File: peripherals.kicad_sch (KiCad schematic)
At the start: 9 parts, among them U1 MX6UL-VM

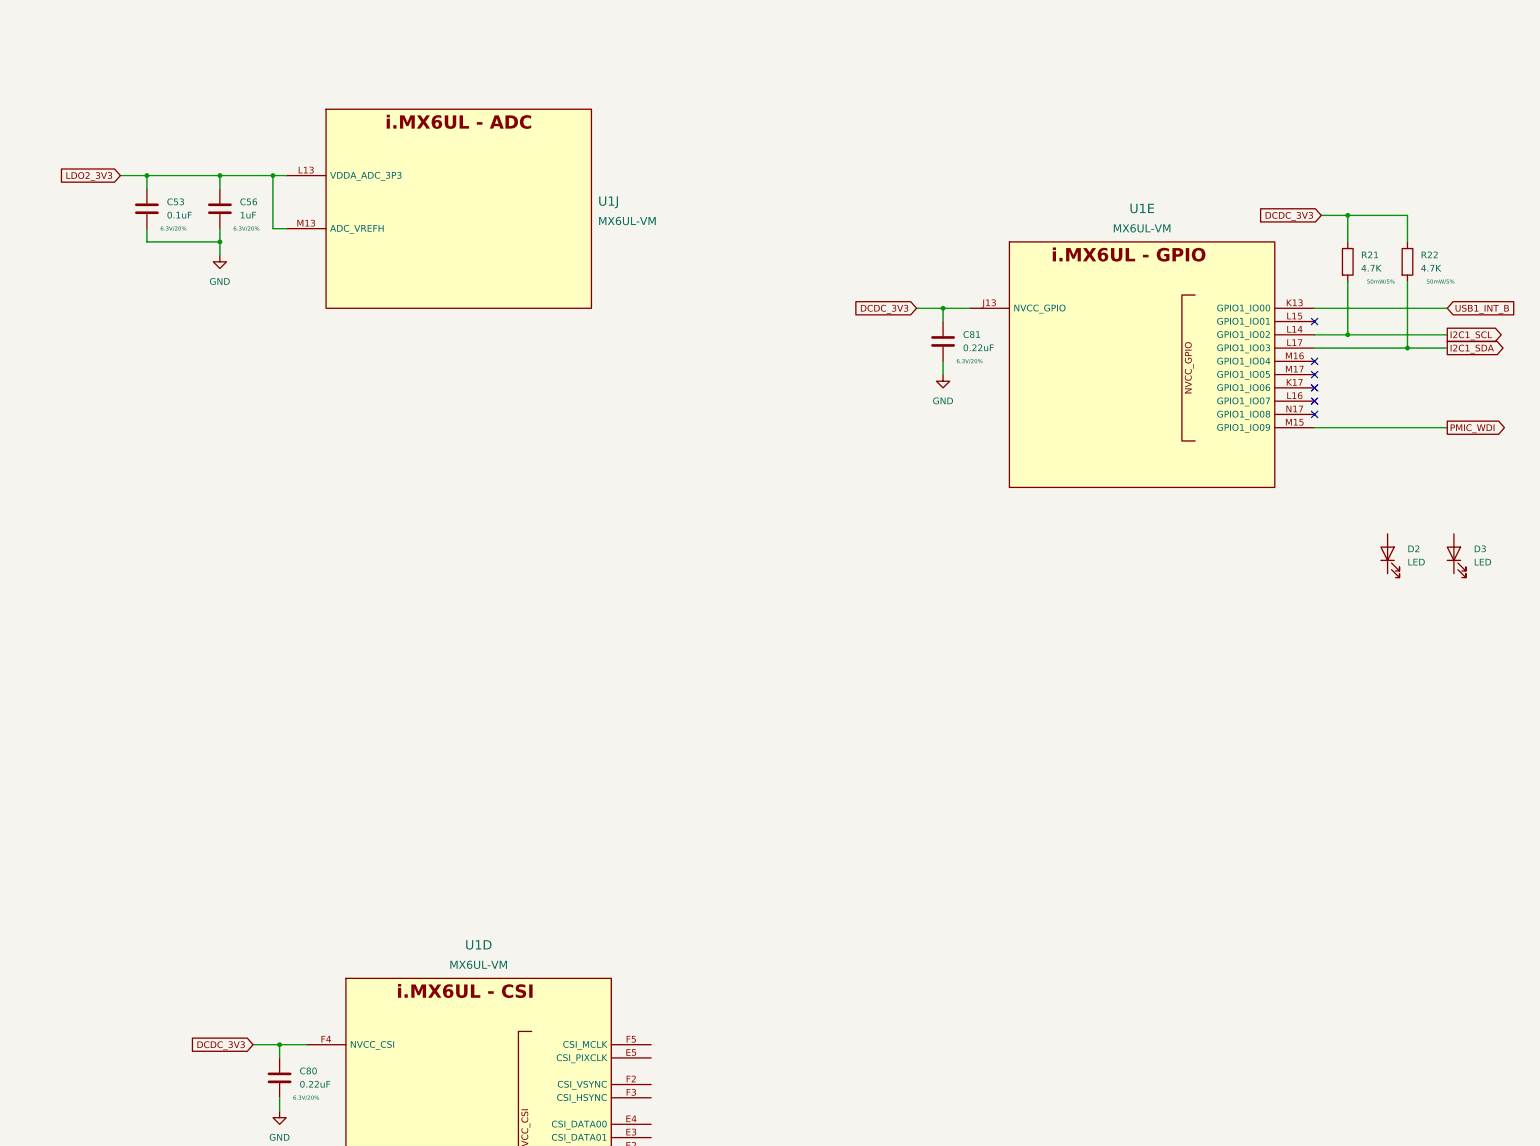
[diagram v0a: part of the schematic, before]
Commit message: start moving to hierarchal labels, add emmc
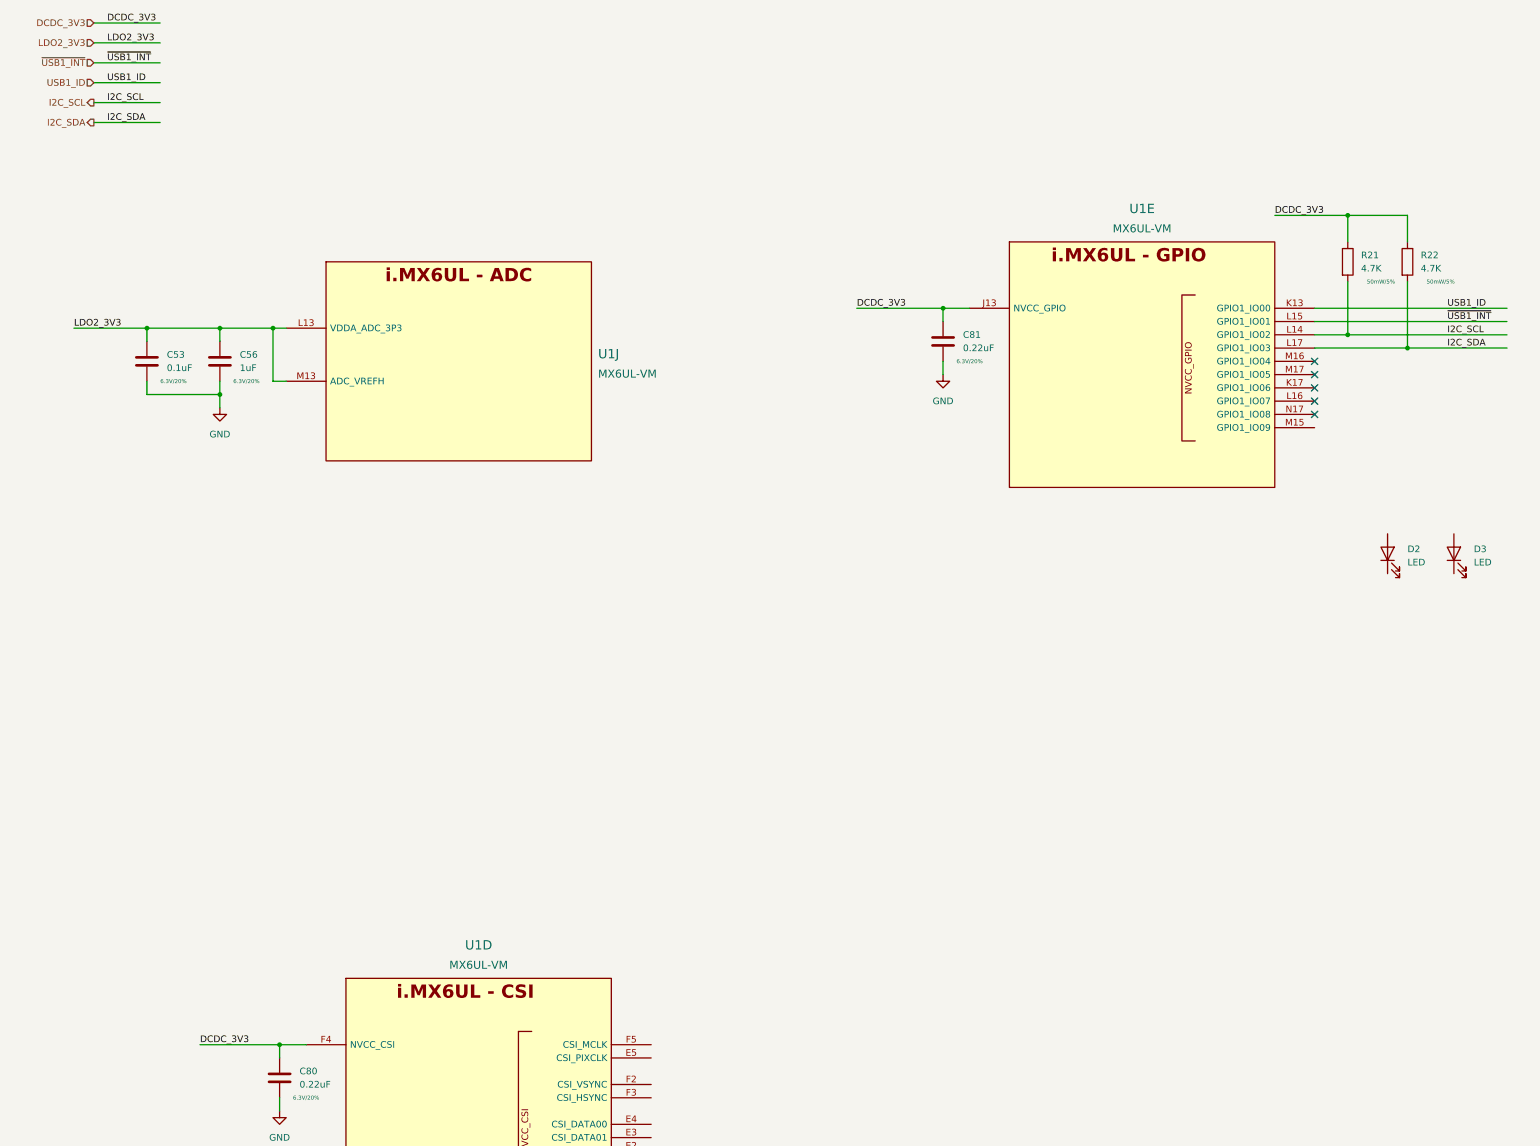
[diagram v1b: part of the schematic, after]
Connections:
- net ~{USB1_INT}: now reaches U1.L15 (GPIO1_IO01)
- net I2C1_SCL renamed I2C_SCL
- net I2C1_SDA renamed I2C_SDA
- net PMIC_WDI: no longer names the net of U1.M15 (GPIO1_IO09)
- net USB1_INT_B renamed USB1_ID
- no-connect marks 6 -> 5
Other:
- moved on the sheet: C53, C56, U1J

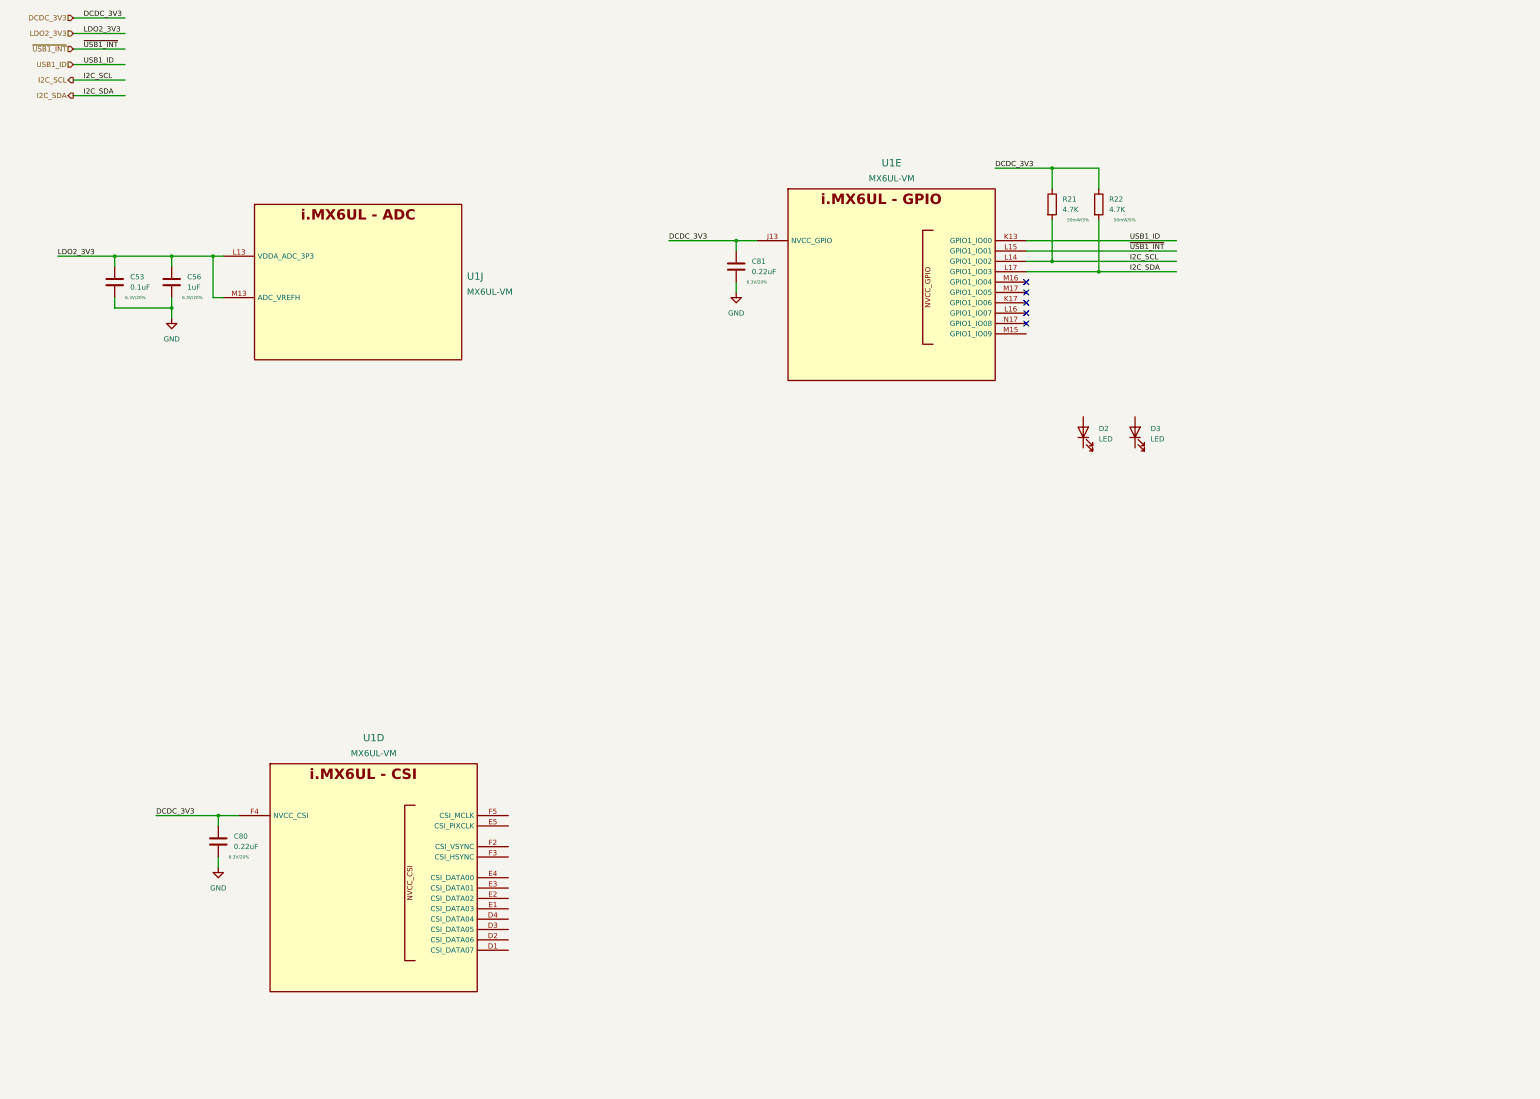
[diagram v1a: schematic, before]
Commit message: move to hierarchal labels, work on power tree, add basic pcb layout
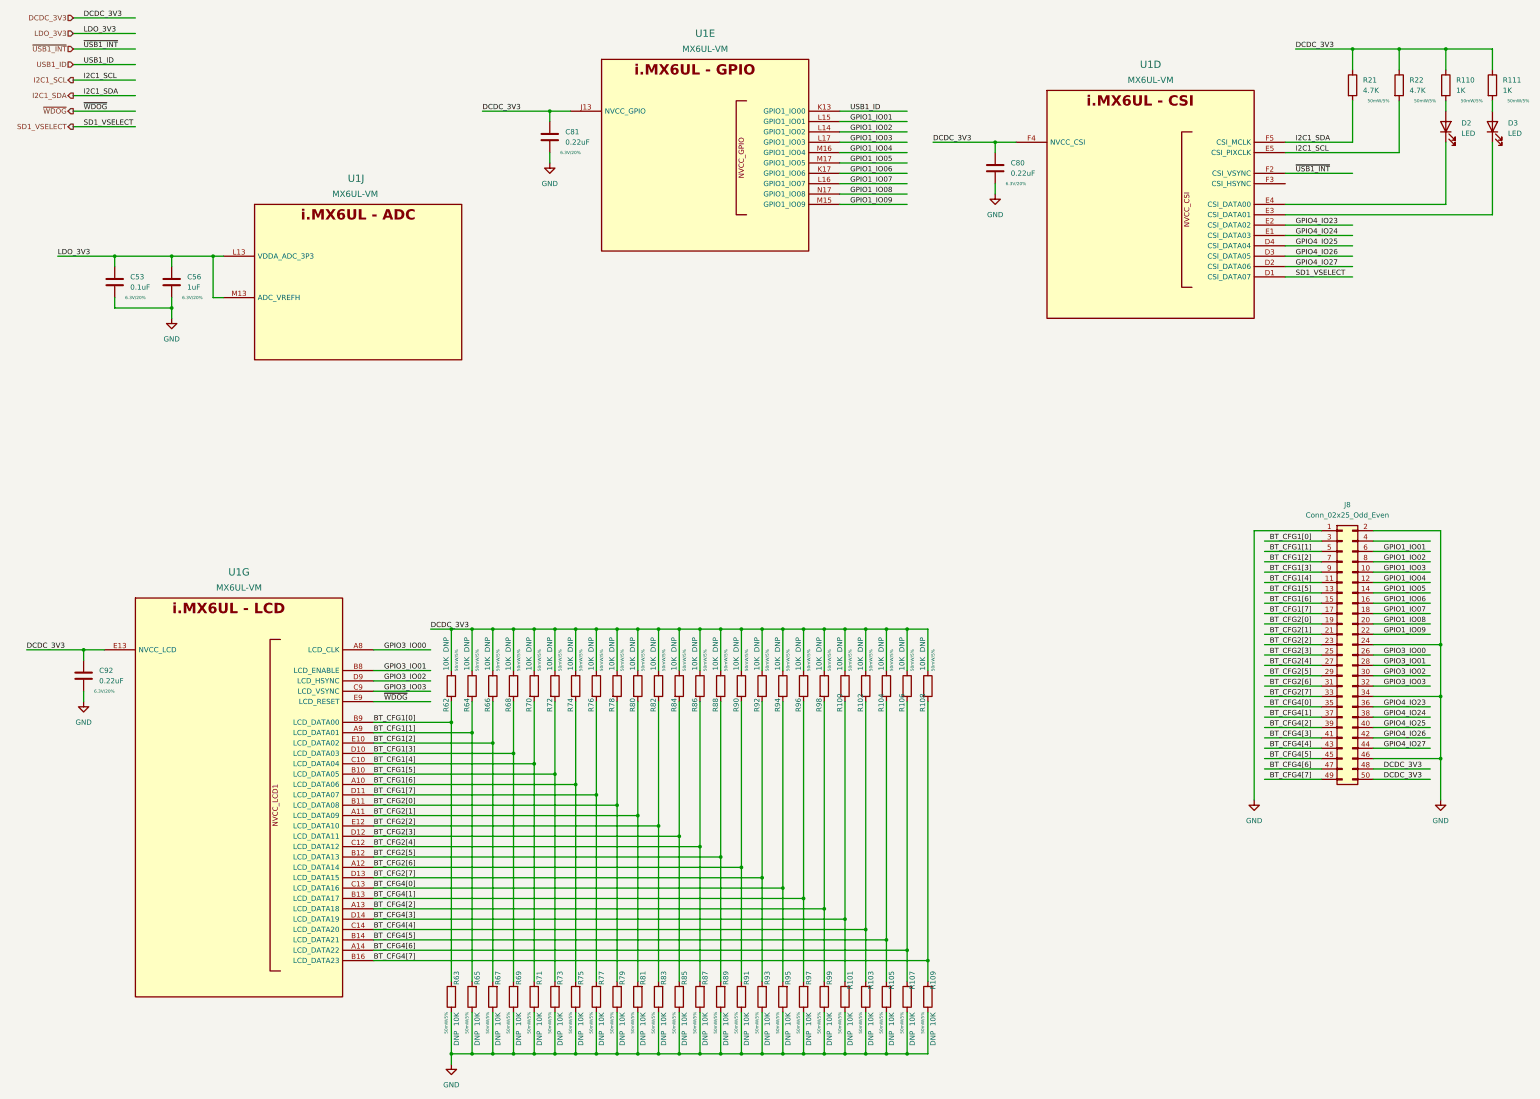
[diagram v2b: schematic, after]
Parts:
- added C92: 0.22uF, Capacitor_SMD:C_0402_1005Metric, symbol Device:C
- added J8: Conn_02x25_Odd_Even, Connector_PinHeader_2.54mm:PinHeader_2x25_P2.54mm_Vertical_SMD, symbol Connector_Generic:Conn_02x25_Odd_Even
- added R100, R101, R102, R103, R104, R105, R106, R107, R108, R109, R62, R63, R64, R65, R66, R67, R68, R69, R70, R71, R72, R73, R74, R75, R76, R77, R78, R79, R80, R81, R82, R83, R84, R85, R86, R87, R88, R89, R90, R91, R92, R93, R94, R95, R96, R97, R98, R99: 10K, Resistor_SMD:R_0402_1005Metric, symbol Device:R
- added R110, R111: 1K, Resistor_SMD:R_0402_1005Metric, symbol Device:R
- added unit 7 of U1
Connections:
- net DCDC_3V3: now also C92.1, J8.48 (Pin_48), J8.50 (Pin_50), R100.1, R102.1, R104.1, R106.1, R108.1, R110.1, R111.1, R62.1, R64.1, R66.1, R68.1, R70.1, R72.1, R74.1, R76.1, R78.1, R80.1, R82.1, R84.1, R86.1, R88.1, R90.1, R92.1, R94.1, R96.1, R98.1, U1.E13 (NVCC_LCD)
- net GND: now also C92.2, J8.1 (Pin_1), J8.2 (Pin_2), J8.24 (Pin_24), J8.34 (Pin_34), J8.46 (Pin_46), R101.1, R103.1, R105.1, R107.1, R109.1, R63.1, R65.1, R67.1, R69.1, R71.1, R73.1, R75.1, R77.1, R79.1, R81.1, R83.1, R85.1, R87.1, R89.1, R91.1, R93.1, R95.1, R97.1, R99.1
- net ~{USB1_INT}: now also U1.F2 (CSI_VSYNC); no longer U1.L15 (GPIO1_IO01)
- net SD1_VSELECT: now reaches U1.D1 (CSI_DATA07)
- net GPIO4_IO27: now reaches U1.D2 (CSI_DATA06)
- net GPIO4_IO27: now also J8.44 (Pin_44)
- net GPIO4_IO26: now reaches U1.D3 (CSI_DATA05)
- net GPIO4_IO26: now also J8.42 (Pin_42)
- net GPIO4_IO25: now reaches U1.D4 (CSI_DATA04)
- net GPIO4_IO25: now also J8.40 (Pin_40)
- net GPIO4_IO24: now reaches U1.E1 (CSI_DATA03)
- net GPIO4_IO24: now also J8.38 (Pin_38)
- net GPIO4_IO23: now reaches U1.E2 (CSI_DATA02)
- net GPIO4_IO23: now also J8.36 (Pin_36)
- net at U1.E3 (CSI_DATA01): now also D3.1 (K)
- net at U1.E4 (CSI_DATA00): now also D2.1 (K)
- net I2C1_SCL: now reaches U1.E5 (CSI_PIXCLK)
- net I2C1_SCL: now also R22.2
- net I2C1_SDA: now reaches U1.F5 (CSI_MCLK)
- net I2C1_SDA: now also R21.2
- net GPIO1_IO06: now reaches U1.K17 (GPIO1_IO06)
- net GPIO1_IO06: now also J8.16 (Pin_16)
- net GPIO1_IO07: now reaches U1.L16 (GPIO1_IO07)
- net GPIO1_IO07: now also J8.18 (Pin_18)
- net GPIO1_IO09: now reaches U1.M15 (GPIO1_IO09)
- net GPIO1_IO09: now also J8.22 (Pin_22)
- net GPIO1_IO04: now reaches U1.M16 (GPIO1_IO04)
- net GPIO1_IO04: now also J8.12 (Pin_12)
- net GPIO1_IO05: now reaches U1.M17 (GPIO1_IO05)
- net GPIO1_IO05: now also J8.14 (Pin_14)
- net GPIO1_IO08: now reaches U1.N17 (GPIO1_IO08)
- net GPIO1_IO08: now also J8.20 (Pin_20)
- net at D2.2 (A): now also R110.2
- net at D3.2 (A): now also R111.2
- net I2C_SCL renamed GPIO1_IO02
- net GPIO1_IO02: now also J8.8 (Pin_8); no longer R21.2
- net I2C_SDA renamed GPIO1_IO03
- net GPIO1_IO03: now also J8.10 (Pin_10); no longer R22.2
- net LDO2_3V3 renamed LDO_3V3
- new net BT_CFG1[0]: J8.3 (Pin_3), R62.2, R63.2, U1.B9 (LCD_DATA00)
- new net BT_CFG1[1]: J8.5 (Pin_5), R64.2, R65.2, U1.A9 (LCD_DATA01)
- new net BT_CFG1[2]: J8.7 (Pin_7), R66.2, R67.2, U1.E10 (LCD_DATA02)
- new net BT_CFG1[3]: J8.9 (Pin_9), R68.2, R69.2, U1.D10 (LCD_DATA03)
- new net BT_CFG1[4]: J8.11 (Pin_11), R70.2, R71.2, U1.C10 (LCD_DATA04)
- new net BT_CFG1[5]: J8.13 (Pin_13), R72.2, R73.2, U1.B10 (LCD_DATA05)
- new net BT_CFG1[6]: J8.15 (Pin_15), R74.2, R75.2, U1.A10 (LCD_DATA06)
- new net BT_CFG1[7]: J8.17 (Pin_17), R76.2, R77.2, U1.D11 (LCD_DATA07)
- new net BT_CFG2[0]: J8.19 (Pin_19), R78.2, R79.2, U1.B11 (LCD_DATA08)
- new net BT_CFG2[1]: J8.21 (Pin_21), R80.2, R81.2, U1.A11 (LCD_DATA09)
- new net BT_CFG2[2]: J8.23 (Pin_23), R82.2, R83.2, U1.E12 (LCD_DATA10)
- new net BT_CFG2[3]: J8.25 (Pin_25), R84.2, R85.2, U1.D12 (LCD_DATA11)
- new net BT_CFG2[4]: J8.27 (Pin_27), R86.2, R87.2, U1.C12 (LCD_DATA12)
- new net BT_CFG2[5]: J8.29 (Pin_29), R88.2, R89.2, U1.B12 (LCD_DATA13)
- new net BT_CFG2[6]: J8.31 (Pin_31), R90.2, R91.2, U1.A12 (LCD_DATA14)
- new net BT_CFG2[7]: J8.33 (Pin_33), R92.2, R93.2, U1.D13 (LCD_DATA15)
- new net BT_CFG4[0]: J8.35 (Pin_35), R94.2, R95.2, U1.C13 (LCD_DATA16)
- new net BT_CFG4[1]: J8.37 (Pin_37), R96.2, R97.2, U1.B13 (LCD_DATA17)
- new net BT_CFG4[2]: J8.39 (Pin_39), R98.2, R99.2, U1.A13 (LCD_DATA18)
- new net BT_CFG4[3]: J8.41 (Pin_41), R100.2, R101.2, U1.D14 (LCD_DATA19)
- new net BT_CFG4[4]: J8.43 (Pin_43), R102.2, R103.2, U1.C14 (LCD_DATA20)
- new net BT_CFG4[5]: J8.45 (Pin_45), R104.2, R105.2, U1.B14 (LCD_DATA21)
- new net BT_CFG4[6]: J8.47 (Pin_47), R106.2, R107.2, U1.A14 (LCD_DATA22)
- new net BT_CFG4[7]: J8.49 (Pin_49), R108.2, R109.2, U1.B16 (LCD_DATA23)
- new net GPIO1_IO01: J8.6 (Pin_6), U1.L15 (GPIO1_IO01)
- new net GPIO3_IO00: J8.26 (Pin_26), U1.A8 (LCD_CLK)
- new net GPIO3_IO01: J8.28 (Pin_28), U1.B8 (LCD_ENABLE)
- new net GPIO3_IO02: J8.30 (Pin_30), U1.D9 (LCD_HSYNC)
- new net GPIO3_IO03: J8.32 (Pin_32), U1.C9 (LCD_VSYNC)
- new net ~{WDOG}: U1.E9 (LCD_RESET)
- no-connect marks 5 -> 0
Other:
- moved on the sheet: C80, C81, D2, D3, R21, R22, U1D, U1E
